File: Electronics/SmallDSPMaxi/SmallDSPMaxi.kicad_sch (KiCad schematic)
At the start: 93 parts, among them J1 Programming, J12 Header, J13 Header, J14 Header, J15 Header, J16 Header, J17 Header, J18 Header, J19 Header, J20 Header, J21 Header, Q1 NSS1C300ET4G, SW1 CJS-1201TB, SW2 CJS-1201TB, SW3 TS-1187A-B-A-B, SW4 CJS-1201TB, U1 ADAU1463, U2 ADM811, U3 M95M01-R, Y1 830105957509

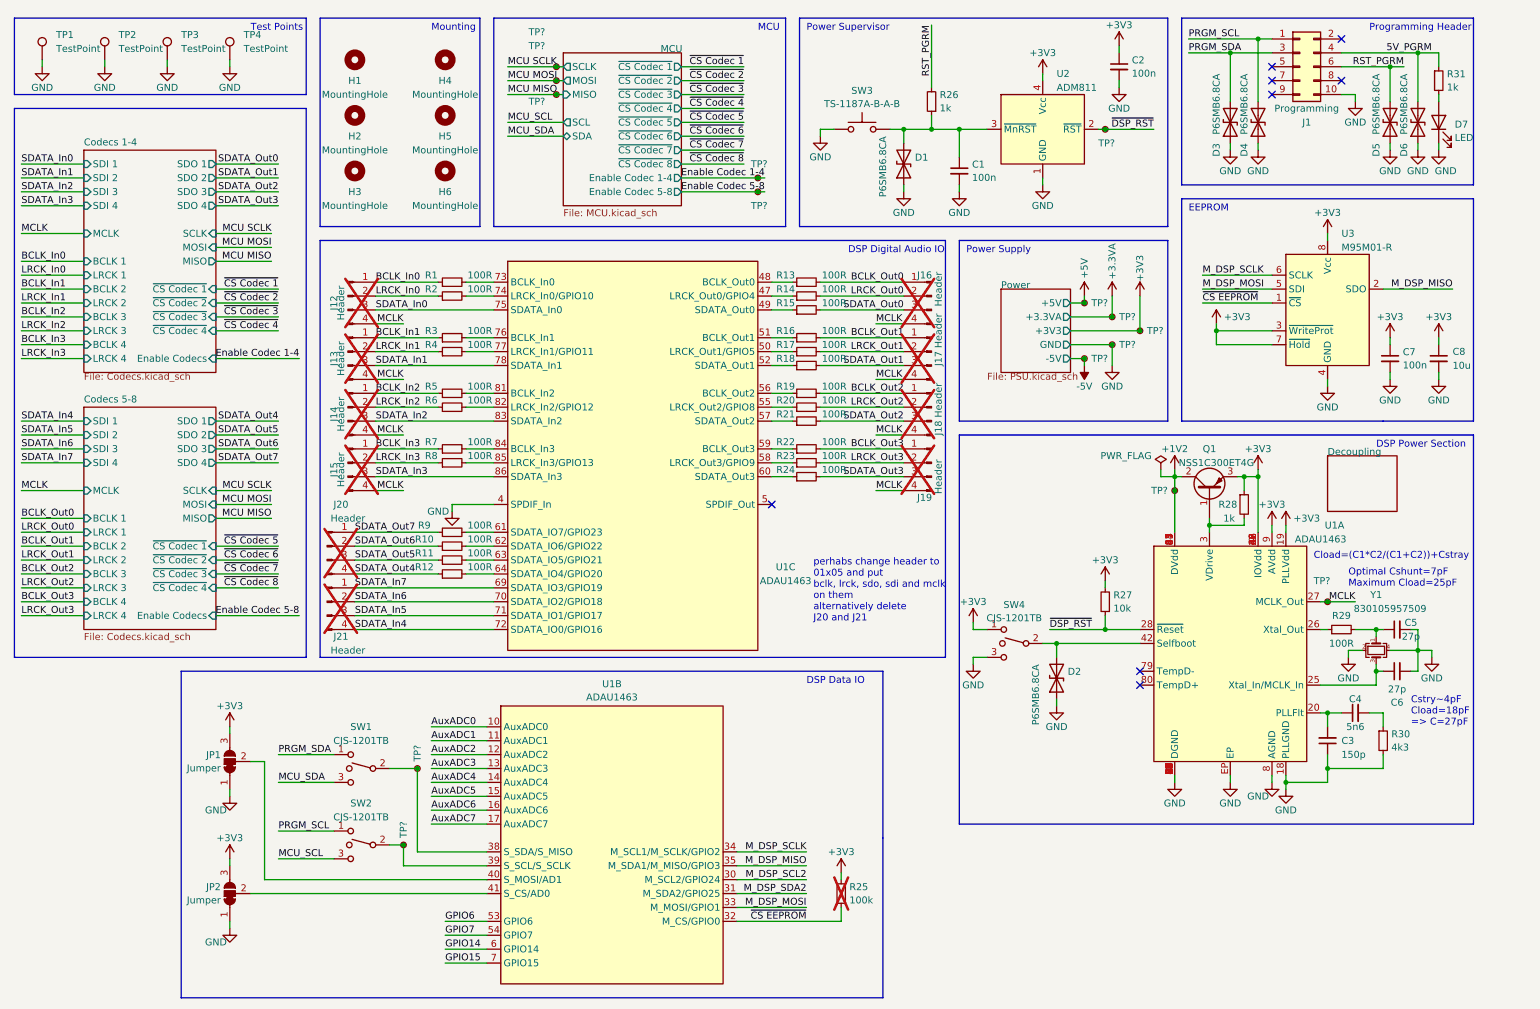
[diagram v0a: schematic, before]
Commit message: Finishes SmallDSP Maxi plus the fitting In- and Output Boards
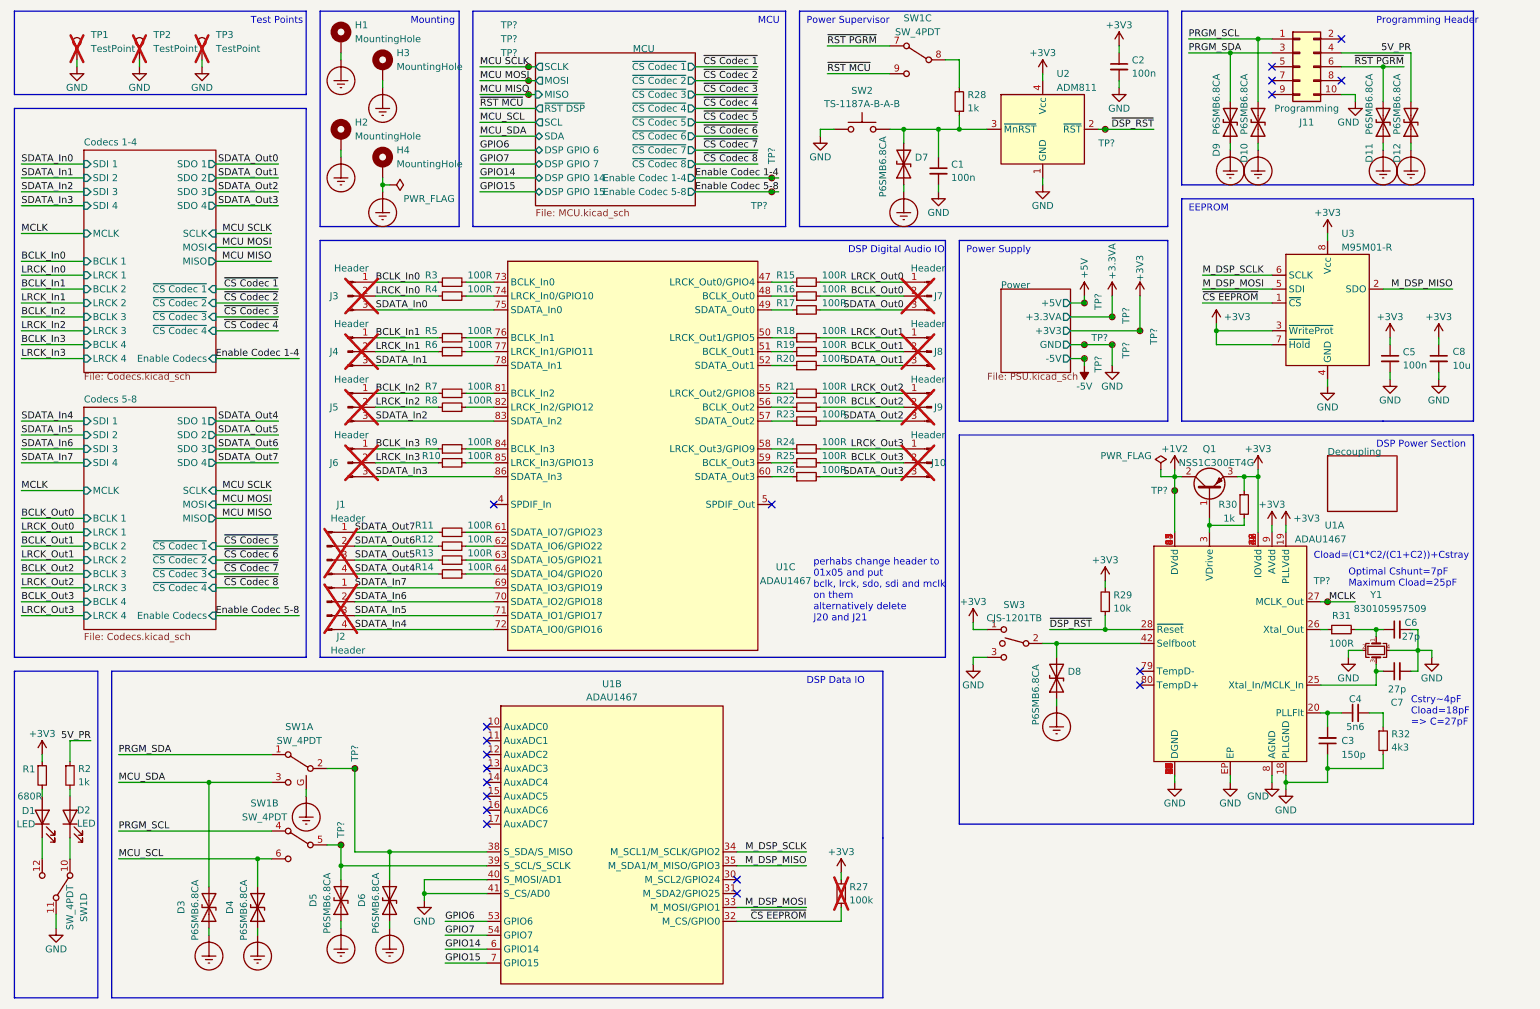
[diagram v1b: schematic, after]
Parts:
- removed H1, H2, H3, H4, H5, H6: MountingHole, MountingHole:MountingHole_3.2mm_M3_ISO7380, symbol Mechanical:MountingHole
- removed J12, J13, J14, J15, J16, J17, J18, J19: Header, Connector_PinHeader_1.27mm:PinHeader_1x04_P1.27mm_Vertical, symbol Connector:Conn_01x04_Pin
- removed JP1, JP2: Jumper, Jumper:SolderJumper-3_P1.3mm_Bridged12_RoundedPad1.0x1.5mm, symbol Jumper:SolderJumper_3_Bridged12
- removed SW1, SW2: CJS-1201TB, 1_Project_Footprints:CJS-1201TB, symbol Switch:SW_SPDT_MSM
- removed TP4: TestPoint, 1_Project_Footprints:TestPoint_Keystone_5019_Minature, symbol Connector:TestPoint
- added D1: LED, Connector_PinHeader_1.27mm:PinHeader_1x02_P1.27mm_Vertical, symbol Device:LED
- added D3, D4, D5, D6: P6SMB6.8CA, Diode_SMD:D_SMB, symbol Device:D_TVS
- added H1, H2, H3, H4: MountingHole, MountingHole:MountingHole_3.2mm_M3_Pad_Via, symbol Mechanical:MountingHole_Pad
- added J10, J3, J4, J5, J6, J7, J8, J9: Header, Connector_PinHeader_1.27mm:PinHeader_1x03_P1.27mm_Vertical, symbol Connector:Conn_01x03_Pin
- added R1: 680R, Resistor_SMD:R_0402_1005Metric, symbol Device:R_Small
- added SW1: SW_4PDT, 1_Project_Footprints:EG4208, symbol 1_Project_Symbols:SW_4PDT
- added TP?: TestPoint, TestPoint:TestPoint_Pad_D1.0mm, symbol Connector:TestPoint_Small
- C1, C2: JLC Part Number C307331 -> (none); LCSC Part # (none) -> C307331
- C3: JLC Part Number C1527 -> (none); LCSC Part # (none) -> C1527
- C4, Q1, TP? (x15), U2, U3, Y1: LCSC Part # (none) -> -
- C5: renamed from C7; JLC Part Number C307331 -> (none); LCSC Part # (none) -> C307331
- C6: renamed from C5; JLC Part Number C1557 -> (none); LCSC Part # (none) -> C1557
- C7: renamed from C6; JLC Part Number C1557 -> (none); LCSC Part # (none) -> C1557
- C8: JLC Part Number C96446 -> (none); LCSC Part # (none) -> C96446
- D10: renamed from D4; JLC Part Number C78395 -> (none); LCSC Part # (none) -> C78395
- D11: renamed from D5; JLC Part Number C78395 -> (none); LCSC Part # (none) -> C78395
- D12: renamed from D6; JLC Part Number C78395 -> (none); LCSC Part # (none) -> C78395
- D2: renamed from D7; footprint LED_SMD:LED_0603_1608Metric -> Connector_PinHeader_1.27mm:PinHeader_1x02_P1.27mm_Vertical; JLC Part Number C72041 -> (none); LCSC Part # (none) -> C72041
- D7: renamed from D1; JLC Part Number C78395 -> (none); LCSC Part # (none) -> C78395
- D8: renamed from D2; JLC Part Number C78395 -> (none); LCSC Part # (none) -> C78395
- D9: renamed from D3; JLC Part Number C78395 -> (none); LCSC Part # (none) -> C78395
- J1: renamed from J20; LCSC Part # (none) -> -; Manufacturer (none) -> -; Part Number (none) -> -
- J11: renamed from J1; LCSC Part # (none) -> -
- J2: renamed from J21; LCSC Part # (none) -> -; Manufacturer (none) -> -; Part Number (none) -> -
- R10: renamed from R8; JLC Part Number C25076 -> (none); LCSC Part # (none) -> C25076
- R11: renamed from R9; JLC Part Number C25076 -> (none); LCSC Part # (none) -> C25076
- R12: renamed from R10; JLC Part Number C25076 -> (none); LCSC Part # (none) -> C25076
- R13: renamed from R11; JLC Part Number C25076 -> (none); LCSC Part # (none) -> C25076
- R14: renamed from R12; JLC Part Number C25076 -> (none); LCSC Part # (none) -> C25076
- R15: renamed from R13; JLC Part Number C25076 -> (none); LCSC Part # (none) -> C25076
- R16: renamed from R14; JLC Part Number C25076 -> (none); LCSC Part # (none) -> C25076
- R17: renamed from R15; JLC Part Number C25076 -> (none); LCSC Part # (none) -> C25076
- R18: renamed from R16; JLC Part Number C25076 -> (none); LCSC Part # (none) -> C25076
- R19: renamed from R17; JLC Part Number C25076 -> (none); LCSC Part # (none) -> C25076
- R2: renamed from R31; JLC Part Number C11702 -> (none); LCSC Part # (none) -> C11702
- R20: renamed from R18; JLC Part Number C25076 -> (none); LCSC Part # (none) -> C25076
- R21: renamed from R19; JLC Part Number C25076 -> (none); LCSC Part # (none) -> C25076
- R22: renamed from R20; JLC Part Number C25076 -> (none); LCSC Part # (none) -> C25076
- R23: renamed from R21; JLC Part Number C25076 -> (none); LCSC Part # (none) -> C25076
- R24: renamed from R22; JLC Part Number C25076 -> (none); LCSC Part # (none) -> C25076
- R25: renamed from R23; JLC Part Number C25076 -> (none); LCSC Part # (none) -> C25076
- R26: renamed from R24; JLC Part Number C25076 -> (none); LCSC Part # (none) -> C25076
- R27: renamed from R25; JLC Part Number C25741 -> (none); LCSC Part # (none) -> C25741
- R28: renamed from R26; JLC Part Number C11702 -> (none); LCSC Part # (none) -> C11702
- R29: renamed from R27; JLC Part Number C25744 -> (none); LCSC Part # (none) -> C25744
- R3: renamed from R1; JLC Part Number C25076 -> (none); LCSC Part # (none) -> C25076
- R30: renamed from R28; JLC Part Number C11702 -> (none); LCSC Part # (none) -> C11702
- R31: renamed from R29; JLC Part Number C25076 -> (none); LCSC Part # (none) -> C25076
- R32: renamed from R30; JLC Part Number C23159 -> (none); LCSC Part # (none) -> C23159
- R4: renamed from R2; JLC Part Number C25076 -> (none); LCSC Part # (none) -> C25076
- R5: renamed from R3; JLC Part Number C25076 -> (none); LCSC Part # (none) -> C25076
- R6: renamed from R4; JLC Part Number C25076 -> (none); LCSC Part # (none) -> C25076
- R7: renamed from R5; JLC Part Number C25076 -> (none); LCSC Part # (none) -> C25076
- R8: renamed from R6; JLC Part Number C25076 -> (none); LCSC Part # (none) -> C25076
- R9: renamed from R7; JLC Part Number C25076 -> (none); LCSC Part # (none) -> C25076
- SW2: renamed from SW3; JLC Part Number C318884 -> (none); LCSC Part # (none) -> C318884
- SW3: renamed from SW4; LCSC Part # (none) -> -
- TP1, TP2, TP3: LCSC Part # (none) -> -; now not fitted
- U1: value ADAU1463 -> ADAU1467; LCSC Part # (none) -> -; Part Number ADAU1463WBCPZ150 -> ADAU1463
- U1: value ADAU1463 -> ADAU1467; LCSC Part # (none) -> -; Part Number ADAU1463WBCPZ150 -> ADAU1467WBCPZ300
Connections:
- net +3V3: now also R1.1
- net BCLK_In0: now also J3.1 (Pin_1)
- net BCLK_In1: now also J4.1 (Pin_1)
- net BCLK_In2: now also J5.1 (Pin_1)
- net BCLK_In3: now also J6.1 (Pin_1)
- net BCLK_Out0: now also R16.2, J7.2 (Pin_2); no longer R15.2
- net BCLK_Out1: now also R19.2, J8.2 (Pin_2); no longer R18.2
- net BCLK_Out2: now also R22.2, J9.2 (Pin_2); no longer R21.2
- net BCLK_Out3: now also R25.2, J10.2 (Pin_2); no longer R24.2
- net GND: now also U1.40 (S_MOSI/AD1), U1.41 (S_CS/AD0), SW1.11 (B), TP?.1; no longer D10.1 (A1), D11.1 (A1), D12.1 (A1), D2.1 (K), D7.1 (A1), D8.1 (A1), D9.1 (A1), U1.4 (SPDIF_In)
- net LRCK_In0: now also J3.2 (Pin_2)
- net LRCK_In1: now also J4.2 (Pin_2)
- net LRCK_In2: now also J5.2 (Pin_2)
- net LRCK_In3: now also J6.2 (Pin_2)
- net LRCK_Out0: now also R15.2, J7.1 (Pin_1); no longer R16.2
- net LRCK_Out1: now also R18.2, J8.1 (Pin_1); no longer R19.2
- net LRCK_Out2: now also R21.2, J9.1 (Pin_1); no longer R22.2
- net LRCK_Out3: now also R24.2, J10.1 (Pin_1); no longer R25.2
- net MCU_SCL: now also D4.2 (A2), SW1.6 (C)
- net MCU_SDA: now also D3.2 (A2), SW1.3 (C)
- net PRGM_SCL: now also SW1.4 (A)
- net PRGM_SDA: now also SW1.1 (A)
- net SDATA_In0: now also J3.3 (Pin_3)
- net SDATA_In1: now also J4.3 (Pin_3)
- net SDATA_In2: now also J5.3 (Pin_3)
- net SDATA_In3: now also J6.3 (Pin_3)
- net SDATA_Out0: now also J7.3 (Pin_3)
- net SDATA_Out1: now also J8.3 (Pin_3)
- net SDATA_Out2: now also J9.3 (Pin_3)
- net SDATA_Out3: now also J10.3 (Pin_3)
- net at R15.1: now also U1.47 (LRCK_Out0/GPIO4); no longer U1.48 (BCLK_Out0)
- net at R16.1: now also U1.48 (BCLK_Out0); no longer U1.47 (LRCK_Out0/GPIO4)
- net at U1.50 (LRCK_Out1/GPIO5): now also R18.1; no longer R19.1
- net at U1.51 (BCLK_Out1): now also R19.1; no longer R18.1
- net at U1.55 (LRCK_Out2/GPIO8): now also R21.1; no longer R22.1
- net at U1.56 (BCLK_Out2): now also R22.1; no longer R21.1
- net at U1.58 (LRCK_Out3/GPIO9): now also R24.1; no longer R25.1
- net at U1.59 (BCLK_Out3): now also R25.1; no longer R24.1
- net at TP?.1, U1.38 (S_SDA/S_MISO): now also D6.2 (A2), SW1.2 (B)
- net at TP?.1, U1.39 (S_SCL/S_SCLK): now also D5.2 (A2), SW1.5 (B)
- net 5V_PGRM renamed 5V_PR
- net AuxADC0: no longer names the net of U1.10 (AuxADC0)
- net AuxADC1: no longer names the net of U1.11 (AuxADC1)
- net AuxADC2: no longer names the net of U1.12 (AuxADC2)
- net AuxADC3: no longer names the net of U1.13 (AuxADC3)
- net AuxADC4: no longer names the net of U1.14 (AuxADC4)
- net AuxADC5: no longer names the net of U1.15 (AuxADC5)
- net AuxADC6: no longer names the net of U1.16 (AuxADC6)
- net AuxADC7: no longer names the net of U1.17 (AuxADC7)
- net M_DSP_SCL2: no longer names the net of U1.30 (M_SCL2/GPIO24)
- net M_DSP_SDA2: no longer names the net of U1.31 (M_SDA2/GPIO25)
- net RST_PGRM renamed ~{RST PGRM}
- net ~{RST PGRM}: now also SW1.7 (A); no longer R28.2
- new net: R28.2, SW1.8 (B)
- new net: D2.1 (K), SW1.10 (A)
- new net: D1.1 (K), SW1.12 (C)
- new net: D1.2 (A), R1.2
- new net Earth_Protective: D10.1 (A1), D11.1 (A1), D12.1 (A1), D3.1 (A1), D4.1 (A1), D5.1 (A1), D6.1 (A1), D7.1 (A1), D8.1 (A1), D9.1 (A1), H1.1, H2.1, H3.1, H4.1, SW1.G
- new net ~{RST MCU}: SW1.9 (C)
- no-connect marks 8 -> 19
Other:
- sheet MCU ports: added DSP GPIO 14, DSP GPIO 15, DSP GPIO 6, DSP GPIO 7, ~{RST DSP}; removed none
- moved on the sheet: C1, D11, D12, D2, R2, R28, TP?

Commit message: replaces 12pin IDC out header with 14pin one because of better availability.
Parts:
- D1, D2: LCSC Part # C72041 -> -; Manufacturer Everlight Elec -> -; Part Number 19-217/BHC-ZL1M2RY/3T -> -
- J10, J3, J4, J5, J6, J7, J8, J9: LCSC Part # (none) -> -; Manufacturer (none) -> -; Part Number (none) -> -
- SW1: LCSC Part # (none) -> -; Manufacturer (none) -> E-Switch; Part Number (none) -> EG4208A
- U1: Part Number ADAU1463 -> ADAU1467WBCPZ300
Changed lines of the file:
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@@
       (effects (font (size 1.27 1.27)) hide)
     )
+    (property "LCSC Part #" "-" (at 182.88 76.2 0)
+      (effects (font (size 1.27 1.27)) hide)
+    )
+    (property "Manufacturer" "-" (at 182.88 76.2 0)
+      (effects (font (size 1.27 1.27)) hide)
+    )
+    (property "Part Number" "-" (at 182.88 76.2 0)
+      (effects (font (size 1.27 1.27)) hide)
+    )
     (pin "1")
     (pin "2")
@@
       (effects (font (size 1.27 1.27)) hide)
     )
+    (property "LCSC Part #" "-" (at 76.2 66.04 0)
+      (effects (font (size 1.27 1.27)) hide)
+    )
+    (property "Manufacturer" "-" (at 76.2 66.04 0)
+      (effects (font (size 1.27 1.27)) hide)
+    )
+    (property "Part Number" "-" (at 76.2 66.04 0)
+      (effects (font (size 1.27 1.27)) hide)
+    )
     (pin "1")
     (pin "2")
@@
       (effects (font (size 1.27 1.27)) hide)
     )
+    (property "LCSC Part #" "-" (at 76.2 96.52 0)
+      (effects (font (size 1.27 1.27)) hide)
+    )
+    (property "Manufacturer" "-" (at 76.2 96.52 0)
+      (effects (font (size 1.27 1.27)) hide)
+    )
+    (property "Part Number" "-" (at 76.2 96.52 0)
+      (effects (font (size 1.27 1.27)) hide)
+    )
     (pin "1")
     (pin "2")
@@
       (effects (font (size 1.27 1.27)) hide)
     )
+    (property "LCSC Part #" "-" (at 180.34 22.86 0)
+      (effects (font (size 1.27 1.27)) hide)
+    )
+    (property "Manufacturer" "E-Switch" (at 180.34 22.86 0)
+      (effects (font (size 1.27 1.27)) hide)
+    )
+    (property "Part Number" "EG4208A" (at 180.34 22.86 0)
+      (effects (font (size 1.27 1.27)) hide)
+    )
     (pin "1")
     (pin "2")
@@
       (effects (font (size 1.27 1.27)) hide)
     )
-    (property "Part Number" "ADAU1463" (at 128.27 55.88 0)
+    (property "Part Number" "ADAU1467WBCPZ300" (at 128.27 55.88 0)
       (effects (font (size 1.27 1.27)) hide)
     )
@@
       (effects (font (size 1.27 1.27)) hide)
     )
+    (property "LCSC Part #" "-" (at 182.88 96.52 0)
+      (effects (font (size 1.27 1.27)) hide)
+    )
+    (property "Manufacturer" "-" (at 182.88 96.52 0)
+      (effects (font (size 1.27 1.27)) hide)
+    )
+    (property "Part Number" "-" (at 182.88 96.52 0)
+      (effects (font (size 1.27 1.27)) hide)
+    )
     (pin "1")
     (pin "2")
@@
       (effects (font (size 1.27 1.27)) hide)
     )
+    (property "LCSC Part #" "-" (at 76.2 86.36 0)
+      (effects (font (size 1.27 1.27)) hide)
+    )
+    (property "Manufacturer" "-" (at 76.2 86.36 0)
+      (effects (font (size 1.27 1.27)) hide)
+    )
+    (property "Part Number" "-" (at 76.2 86.36 0)
+      (effects (font (size 1.27 1.27)) hide)
+    )
     (pin "1")
     (pin "2")
@@
       (effects (font (size 1.27 1.27)) hide)
     )
+    (property "LCSC Part #" "-" (at 76.2 76.2 0)
+      (effects (font (size 1.27 1.27)) hide)
+    )
+    (property "Manufacturer" "-" (at 76.2 76.2 0)
+      (effects (font (size 1.27 1.27)) hide)
+    )
+    (property "Part Number" "-" (at 76.2 76.2 0)
+      (effects (font (size 1.27 1.27)) hide)
+    )
     (pin "1")
     (pin "2")
@@
       (effects (font (size 1.27 1.27)) hide)
     )
+    (property "LCSC Part #" "-" (at 22.86 173.99 0)
+      (effects (font (size 1.27 1.27)) hide)
+    )
+    (property "Manufacturer" "E-Switch" (at 22.86 173.99 0)
+      (effects (font (size 1.27 1.27)) hide)
+    )
+    (property "Part Number" "EG4208A" (at 22.86 173.99 0)
+      (effects (font (size 1.27 1.27)) hide)
+    )
     (pin "1")
     (pin "2")
@@
       (effects (font (size 1.27 1.27)) hide)
     )
+    (property "LCSC Part #" "-" (at 182.88 66.04 0)
+      (effects (font (size 1.27 1.27)) hide)
+    )
+    (property "Manufacturer" "-" (at 182.88 66.04 0)
+      (effects (font (size 1.27 1.27)) hide)
+    )
+    (property "Part Number" "-" (at 182.88 66.04 0)
+      (effects (font (size 1.27 1.27)) hide)
+    )
     (pin "1")
     (pin "2")
@@
       (effects (font (size 1.27 1.27)) hide)
     )
+    (property "LCSC Part #" "-" (at 182.88 86.36 0)
+      (effects (font (size 1.27 1.27)) hide)
+    )
+    (property "Manufacturer" "-" (at 182.88 86.36 0)
+      (effects (font (size 1.27 1.27)) hide)
+    )
+    (property "Part Number" "-" (at 182.88 86.36 0)
+      (effects (font (size 1.27 1.27)) hide)
+    )
     (pin "1")
     (pin "2")
@@
       (effects (font (size 1.27 1.27)) hide)
     )
-    (property "Manufacturer" "Everlight Elec" (at 25.4 161.29 0)
+    (property "Manufacturer" "-" (at 25.4 161.29 0)
       (effects (font (size 1.27 1.27)) hide)
     )
-    (property "Part Number" "19-217/BHC-ZL1M2RY/3T" (at 25.4 161.29 0)
+    (property "Part Number" "-" (at 25.4 161.29 0)
       (effects (font (size 1.27 1.27)) hide)
     )
@@
       (effects (font (size 1.27 1.27)) hide)
     )
-    (property "LCSC Part #" "C72041" (at 25.4 161.29 0)
+    (property "LCSC Part #" "-" (at 25.4 161.29 0)
       (effects (font (size 1.27 1.27)) hide)
     )
@@
       (effects (font (size 1.27 1.27)) hide)
     )
+    (property "LCSC Part #" "-" (at 67.31 152.4 0)
+      (effects (font (size 1.27 1.27)) hide)
+    )
+    (property "Manufacturer" "E-Switch" (at 67.31 152.4 0)
+      (effects (font (size 1.27 1.27)) hide)
+    )
+    (property "Part Number" "EG4208A" (at 67.31 152.4 0)
+      (effects (font (size 1.27 1.27)) hide)
+    )
     (pin "1")
     (pin "2")
@@
       (effects (font (size 1.27 1.27)) hide)
     )
+    (property "LCSC Part #" "-" (at 67.31 166.37 0)
+      (effects (font (size 1.27 1.27)) hide)
+    )
+    (property "Manufacturer" "E-Switch" (at 67.31 166.37 0)
+      (effects (font (size 1.27 1.27)) hide)
+    )
+    (property "Part Number" "EG4208A" (at 67.31 166.37 0)
+      (effects (font (size 1.27 1.27)) hide)
+    )
     (pin "1")
     (pin "2")
@@
       (effects (font (size 1.27 1.27)) hide)
     )
-    (property "Manufacturer" "Everlight Elec" (at 20.32 161.29 0)
+    (property "Manufacturer" "-" (at 20.32 161.29 0)
       (effects (font (size 1.27 1.27)) hide)
     )
-    (property "Part Number" "19-217/BHC-ZL1M2RY/3T" (at 20.32 161.29 0)
+    (property "Part Number" "-" (at 20.32 161.29 0)
       (effects (font (size 1.27 1.27)) hide)
     )
@@
       (effects (font (size 1.27 1.27)) hide)
     )
-    (property "LCSC Part #" "C72041" (at 20.32 161.29 0)
+    (property "LCSC Part #" "-" (at 20.32 161.29 0)
       (effects (font (size 1.27 1.27)) hide)
     )
